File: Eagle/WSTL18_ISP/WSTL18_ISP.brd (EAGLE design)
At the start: 18.4 x 10.2 mm, 2 parts, among them J3 FEMALE 2x3

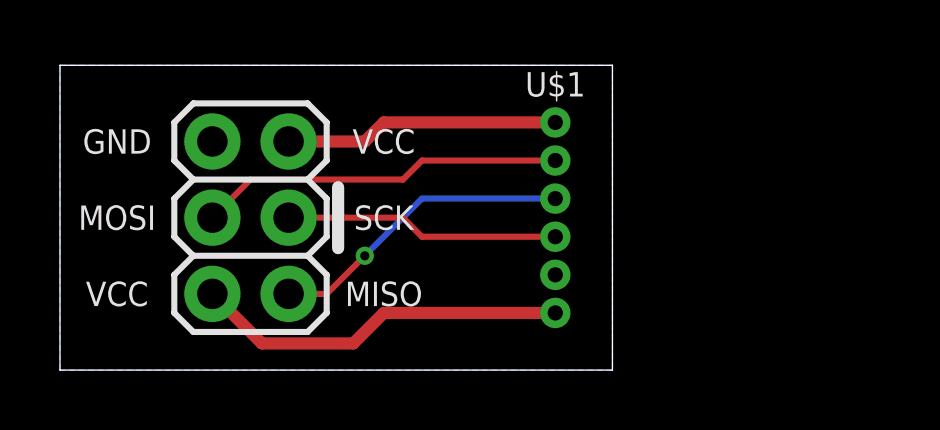
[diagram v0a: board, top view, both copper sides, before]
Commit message: Finished design of WSTL18 in-system programming adaptor
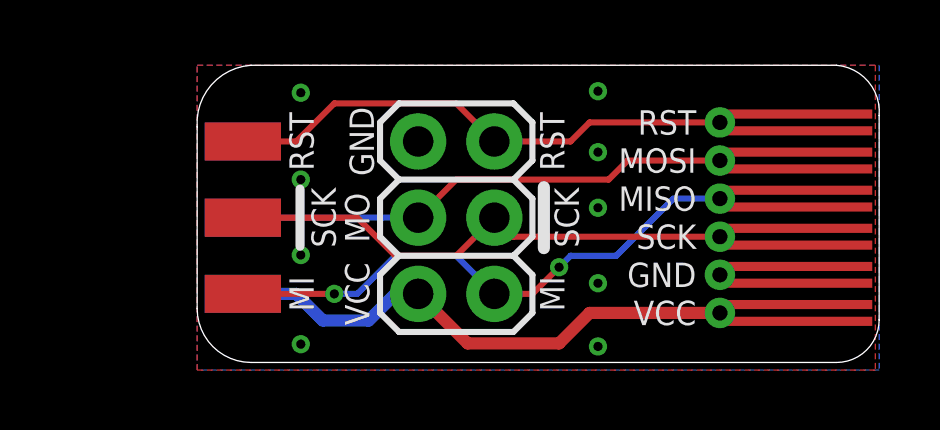
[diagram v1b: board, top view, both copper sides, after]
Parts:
- added U$2: AVR_ISP_6_PIN_SIDE, Connectors:AVR_ISP_SIDE_0.1_INCH
- U$1: value 1X6CONN-1.27-ROUND -> 1X6CONN-1.27-ROUNDPOGO; device AVR_ISP_127:1X6_1.27_ROUND -> AVR_ISP_127:1X6_1.27_SIDEPOGO
- moved J3 6.86 mm to (14.5, 2.54)
- moved U$1 5.49 mm to (22.0, 8.26)
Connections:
- net GND: now also U$1.ROUND5, U$2.GND; no longer U$1.5
- net MISO: now also U$1.ROUND3, U$2.MISO; no longer U$1.3
- net MOSI: now also U$1.ROUND2, U$2.MOSI; no longer U$1.2
- net RESET: now also U$1.ROUND1, U$2.RST; no longer U$1.1
- net SCK: now also U$1.ROUND4, U$2.SCK; no longer U$1.4
- net VCC: now also U$1.ROUND6, U$2.VCC; no longer U$1.6
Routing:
- net MISO: track 10.2 -> 18.3 mm, vias 1 -> 2
- net RESET: track 9.15 -> 17.2 mm
- net SCK: track 9.15 -> 17.2 mm
- net VCC: track 12.5 -> 17.7 mm
- net MOSI: track 12.2 -> 16.7 mm
- added copper zone on layer 1, net GND
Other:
- board size 18.4 x 10.2 mm -> 22.7 x 9.9 mm
- board text added: "AVR ISP CONNECTOR WSTL18"
- board text added: "MI"
- board text added: "MO"
- board text added: "RST"
- board text added: "WILDLIFE SENSE 2018"
